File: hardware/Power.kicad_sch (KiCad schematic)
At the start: 1 part

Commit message: added more stuff wip
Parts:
- added C33, C38: 1u, Capacitor_SMD:C_0603_1608Metric, symbol Device:C
- added C34, C38: 0.1u, Capacitor_SMD:C_0603_1608Metric, symbol Device:C
- added C35: 220n, Capacitor_SMD:C_0603_1608Metric, symbol Device:C
- added C37 (x2): 10u, Capacitor_SMD:C_0805_2012Metric, symbol Device:C
- added D16: SMAF4758A, UTSVT_Passives:SODFL4724X108N, symbol Device:D_Zener
- added IC3: LM74502HDDFR, UTSVT_Power:SOT65P280X110-8N, symbol UTSVT_ICs:LM74502HDDFR
- added LVPWR1: LED, LED_SMD:LED_0603_1608Metric, symbol Device:LED
- added Q12, Q13: NVMFWS1D7N04XMT1G, UTSVT_Power:NVMFWS3D0P04M8LT1G, symbol UTSVT_Power:NVMFWS1D7N04XMT1G
- added R36: 10k, Resistor_SMD:R_0603_1608Metric, symbol Device:R_US
- added R37: 200k, Resistor_SMD:R_0603_1608Metric, symbol Device:R_US
- added R38: 9k, Resistor_SMD:R_0603_1608Metric, symbol Device:R_US
- added R83: 4.3k, Resistor_SMD:R_0603_1608Metric, symbol Device:R_US
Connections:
- net +24V_In renamed LV_OUT
- net LV_OUT: now also C37.1, C37.1, C38.1, Q12.5 (D), Q12.6 (D), Q12.7 (D), Q12.8 (D), Q12.9 (D), R83.1
- net +24V_In_Fused renamed 24V_BPS
- new net: C35.2, IC3.4 (VCAP)
- new net: IC3.6 (GATE), Q12.4 (G), Q13.4 (G)
- new net: IC3.7 (OV), R37.2, R38.1
- new net: IC3.8 (SRC), Q12.1 (S), Q12.2 (S), Q12.3 (S), Q13.1 (S), Q13.2 (S), Q13.3 (S)
- new net: LVPWR1.2 (A), R83.2
- new net GND: C33.1, C34.2, C37.2, C37.2, C38.2, C38.2, D16.2 (A), IC3.2 (GND), LVPWR1.1 (K), R38.2
- new net LV+_IN: C34.1, C38.1, Q13.5 (D), Q13.6 (D), Q13.7 (D), Q13.8 (D), Q13.9 (D), R36.1, R37.1
- new net RPP_EN: C33.2, C35.1, D16.1 (K), IC3.1 (EN/UVLO), IC3.5 (VS), R36.2
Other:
- added sheet Power_3V3Buck (Power_3V3Buck.kicad_sch)
- added sheet Power_Protection (Power_Protection.kicad_sch)
- note added: "24V Input Bypass Cap"
- note added: "Fused 24V to other BPS boards"
- note added: "LV PWR indicator LED"
- note added: "Overvoltage Protection: 29.03V Vovr = (R2 * Vov)/(R1 + R2) Vov = Vovr * (R1 + R2) / R2 29.03 = 1.25 * (200k + 9k) / 9k"
- note added: "RPP Protection"
- moved on the sheet: F1

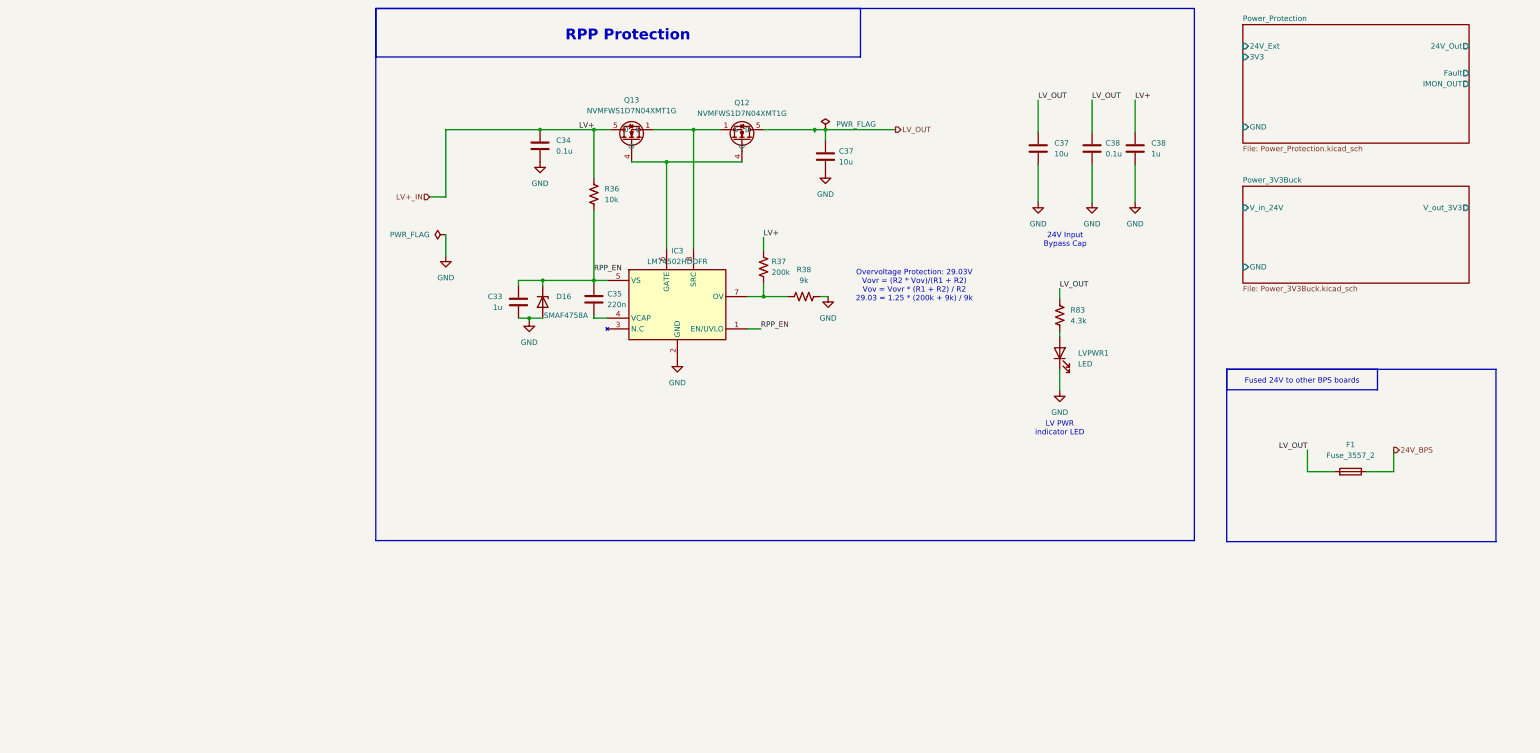
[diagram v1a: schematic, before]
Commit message: some changes - switched to contactor design block - switched to power protection design block - added SD card - added fan I2C pullup - added resistors for ESP32 power mux - shield tied to gnd with 0 ohm - added USB-PD and boost design blocks
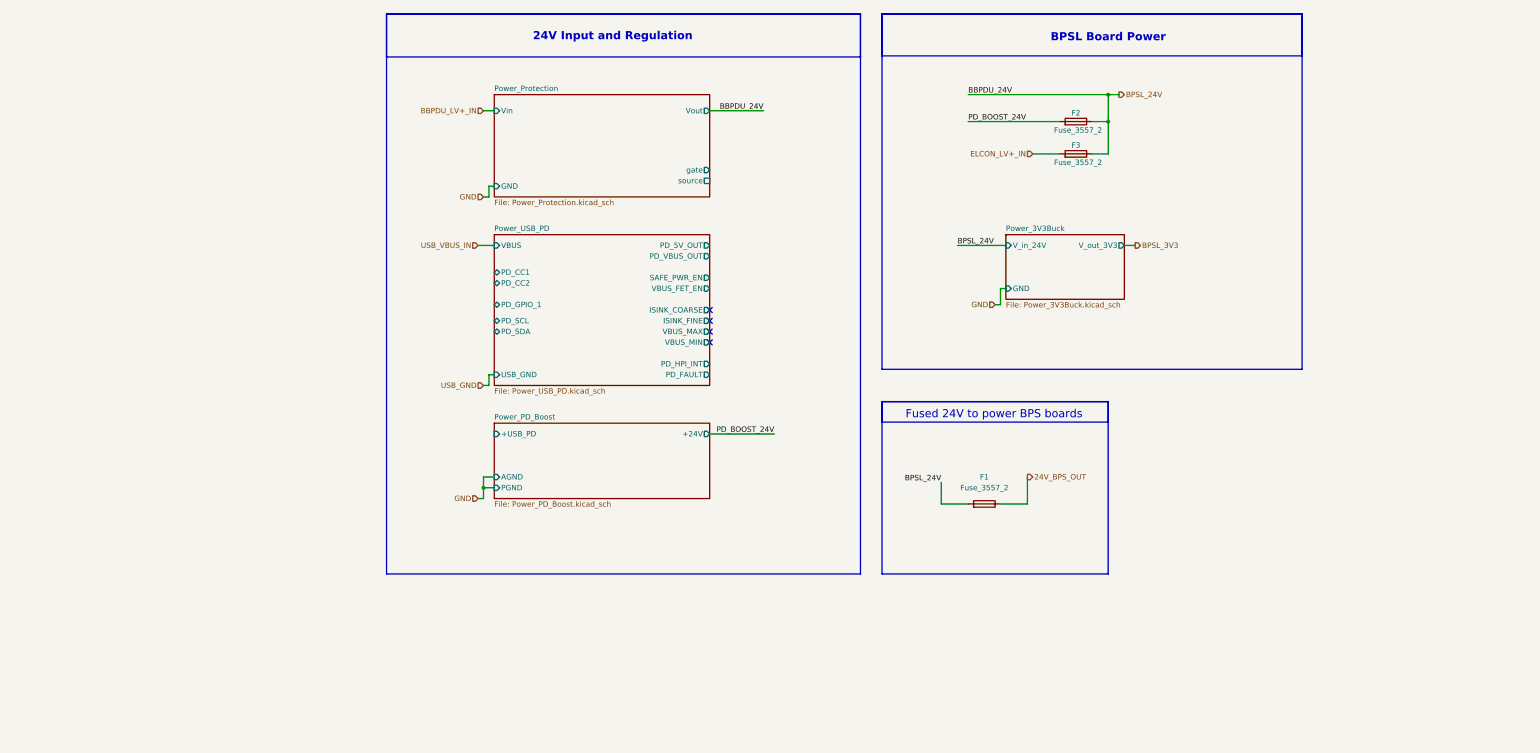
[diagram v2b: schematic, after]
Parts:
- removed C33, C38: 1u, Capacitor_SMD:C_0603_1608Metric, symbol Device:C
- removed C34, C38: 0.1u, Capacitor_SMD:C_0603_1608Metric, symbol Device:C
- removed C35: 220n, Capacitor_SMD:C_0603_1608Metric, symbol Device:C
- removed C37 (x2): 10u, Capacitor_SMD:C_0805_2012Metric, symbol Device:C
- removed D16: SMAF4758A, UTSVT_Passives:SODFL4724X108N, symbol Device:D_Zener
- removed IC3: LM74502HDDFR, UTSVT_Power:SOT65P280X110-8N, symbol UTSVT_ICs:LM74502HDDFR
- removed LVPWR1: LED, LED_SMD:LED_0603_1608Metric, symbol Device:LED
- removed Q12, Q13: NVMFWS1D7N04XMT1G, UTSVT_Power:NVMFWS3D0P04M8LT1G, symbol UTSVT_Power:NVMFWS1D7N04XMT1G
- removed R36: 10k, Resistor_SMD:R_0603_1608Metric, symbol Device:R_US
- removed R37: 200k, Resistor_SMD:R_0603_1608Metric, symbol Device:R_US
- removed R38: 9k, Resistor_SMD:R_0603_1608Metric, symbol Device:R_US
- removed R83: 4.3k, Resistor_SMD:R_0603_1608Metric, symbol Device:R_US
- added F2, F3: Fuse_3557_2, LHRS_Power:Fuse-3557-2, symbol lhrs_power:Fuse_3557_2
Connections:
- net 24V_BPS renamed 24V_BPS_OUT
- net LV_OUT renamed BPSL_24V
- net BPSL_24V: now also F2.2, F3.2
- new net ELCON_LV+_IN: F3.1
- new net PD_BOOST_24V: F2.1
- no-connect marks 0 -> 4
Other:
- added sheet Power_PD_Boost (Power_PD_Boost.kicad_sch)
- added sheet Power_USB_PD (Power_USB_PD.kicad_sch)
- sheet Power_Protection ports: added Vin, Vout, gate, source; removed 24V_Ext, 24V_Out, 3V3, Fault, IMON_OUT
- note added: "24V Input and Regulation"
- note added: "BPSL Board Power"
- note added: "Fused 24V to power BPS boards"
- note removed: "24V Input Bypass Cap"
- note removed: "Fused 24V to other BPS boards"
- note removed: "LV PWR indicator LED"
- note removed: "Overvoltage Protection: 29.03V Vovr = (R2 * Vov)/(R1 + R2) Vov = Vovr * (R1 + R2) / R2 29.03 = 1.25 * (200k + 9k) / 9k"
- note removed: "RPP Protection"
- moved on the sheet: F1

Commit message: power updates
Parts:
- added R28: 16k, symbol Device:R_Small
- added R29: 4.7k, symbol Device:R_Small
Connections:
- net BPSL_24V: no longer F2.2, F3.2
- net GND: now also R29.2
- new net PD_5V_OUT: R28.1
- new net Power_5VMux/PR1: R28.2, R29.1
- no-connect marks 4 -> 0
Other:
- removed sheet Power_3V3Buck
- added sheet Power_3V3_LDO (Power_3V3_LDO.kicad_sch)
- added sheet Power_5VBuck (Power_5VBuck.kicad_sch)
- added sheet Power_5VMux (Power_5VMux.kicad_sch)
- note added: "5V Mux"
- note added: "BPSL Board Power (24V, 3V3)"
- note added: "Mux?"
- note added: "PDU Regulation (RPP)"
- note added: "R1"
- note added: "R2"
- note added: "USB PD + Boost"
- note added: "VIN1 prioritized"
- note removed: "BPSL Board Power"
- moved on the sheet: F1, F2, F3

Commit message: interview tabling
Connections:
- net 24V_BPS_OUT renamed 12V_BPS_OUT
- net BPSL_24V renamed BPSL_12V
- net PD_BOOST_24V renamed PD_12V
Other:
- note added: "((PDU | ELCON) | PD) reasoning: PDU or elcon will be prioritized over PD since it could be being used for debugging. In those events, power from car or elcon is better. since PD needs the lowest priority, it will be one its own input into the highest mux so the other input will have higher priority. then, between PDU and ELCON that mux can prioritize PDU"
- note added: "12V Input and Regulation"
- note added: "BPSL Board Power (12V, 3V3)"
- note added: "Fused 12V to power BPS boards"
- note added: "PD should try to negotiate 12V. Or could just try to negotiate highest possible and rely on buckboost"
- note removed: "24V Input and Regulation"
- note removed: "BPSL Board Power (24V, 3V3)"
- note removed: "Fused 24V to power BPS boards"
- moved on the sheet: R28, R29

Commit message: asdf
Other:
- added sheet 12VPowerMux (Power_Mux_12V.kicad_sch)
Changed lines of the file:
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@@
+	)
+	(sheet
+		(at 111.125 102.87)
+		(size 20.32 20.955)
+		(exclude_from_sim no)
+		(in_bom yes)
+		(on_board yes)
+		(dnp no)
+		(fields_autoplaced yes)
+		(stroke
+			(width 0.1524)
+			(type solid)
+		)
+		(fill
+			(color 0 0 0 0)
+		)
+		(property "Sheetname" "12VPowerMux"
+			(at 111.125 102.1584 0)
+			(show_name no)
+			(do_not_autoplace no)
+			(effects
+				(font
+					(size 1.27 1.27)
+				)
+				(justify left bottom)
+			)
+		)
+		(property "Sheetfile" "Power_Mux_12V.kicad_sch"
+			(at 111.125 124.4096 0)
+			(show_name no)
+			(do_not_autoplace no)
+			(effects
+				(font
+					(size 1.27 1.27)
+				)
+				(justify left top)
+			)
+		)
+		(instances
+			(project "PS-BPSLeader"
+				(path "/d4a4ed4f-0983-4aef-b212-0e3284ab3963/69244dac-f10b-499c-a2b2-3cdf1370aa1f"
+					(page "10")
+				)
+			)
+		)
 	)
 	(sheet

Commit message: end of workday
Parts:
- removed F1: Fuse_3557_2, UTSVT_Power:Fuse-3557-2, symbol utsvt_power:Fuse_3557_2
- added TP?: PD_5V, symbol Connector:TestPoint
- added TP?: MUX_12V, symbol Connector:TestPoint
- added TP?: PDU_ELCON, symbol Connector:TestPoint
- added TP?: PD_OUT, symbol Connector:TestPoint
- F2, F3: value Fuse_3557_2 -> 5A
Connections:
- net PD_5V_OUT: now also TP?.1
- net Power_Mux_PDU_ELCON/Vin2: now reaches F3.2
- net Power_Mux_PD/Vin2: now reaches F2.2
- net PD_12V renamed USB_PD_OUT
- net USB_PD_OUT: now also TP?.1
- new net Power_Mux_PD/12V_MUX_OUT: TP?.1
- new net Power_Mux_PD/Vin1: TP?.1
- no-connect marks 0 -> 10
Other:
- sheet 12VPowerMux renamed Power_Mux_PDU_ELCON
- removed sheet Power_5VBuck
- removed sheet Power_PD_Boost
- removed sheet Power_Protection
- added sheet 12VBuck (12VBuck.kicad_sch)
- added sheet Power_Mux_PD (Power_Mux_PD.kicad_sch)
- sheet Power_Mux_PDU_ELCON ports: added 12V_MUX_OUT, GND, Vin1, Vin2; removed none
- note added: "((PDU | ELCON) | PD) reasoning: PDU or elcon will be prioritized over PD since it could be being used for debugging. In those events, power from car or elcon is better. since PD is the lowest priority, it will be one its own input into the highest mux so the other input will have higher priority. then, between PDU and ELCON that mux can prioritize PDU"
- note added: "USB PD"
- note removed: "((PDU | ELCON) | PD) reasoning: PDU or elcon will be prioritized over PD since it could be being used for debugging. In those events, power from car or elcon is better. since PD needs the lowest priority, it will be one its own input into the highest mux so the other input will have higher priority. then, between PDU and ELCON that mux can prioritize PDU"
- note removed: "Fused 12V to power BPS boards"
- note removed: "Mux?"
- note removed: "USB PD + Boost"
- moved on the sheet: F2, F3, R28, R29

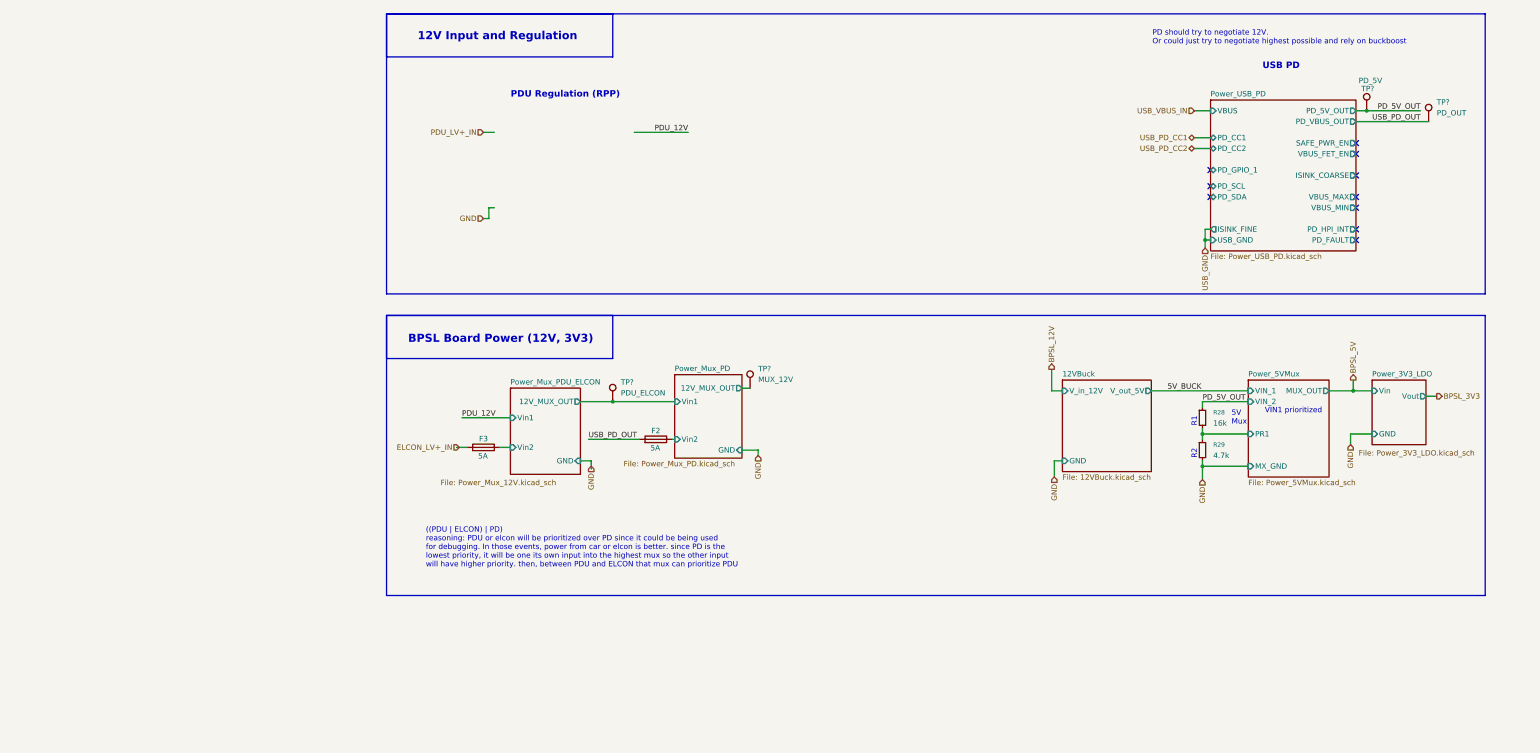
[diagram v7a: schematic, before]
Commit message: finished schematic except for 12v buck boost
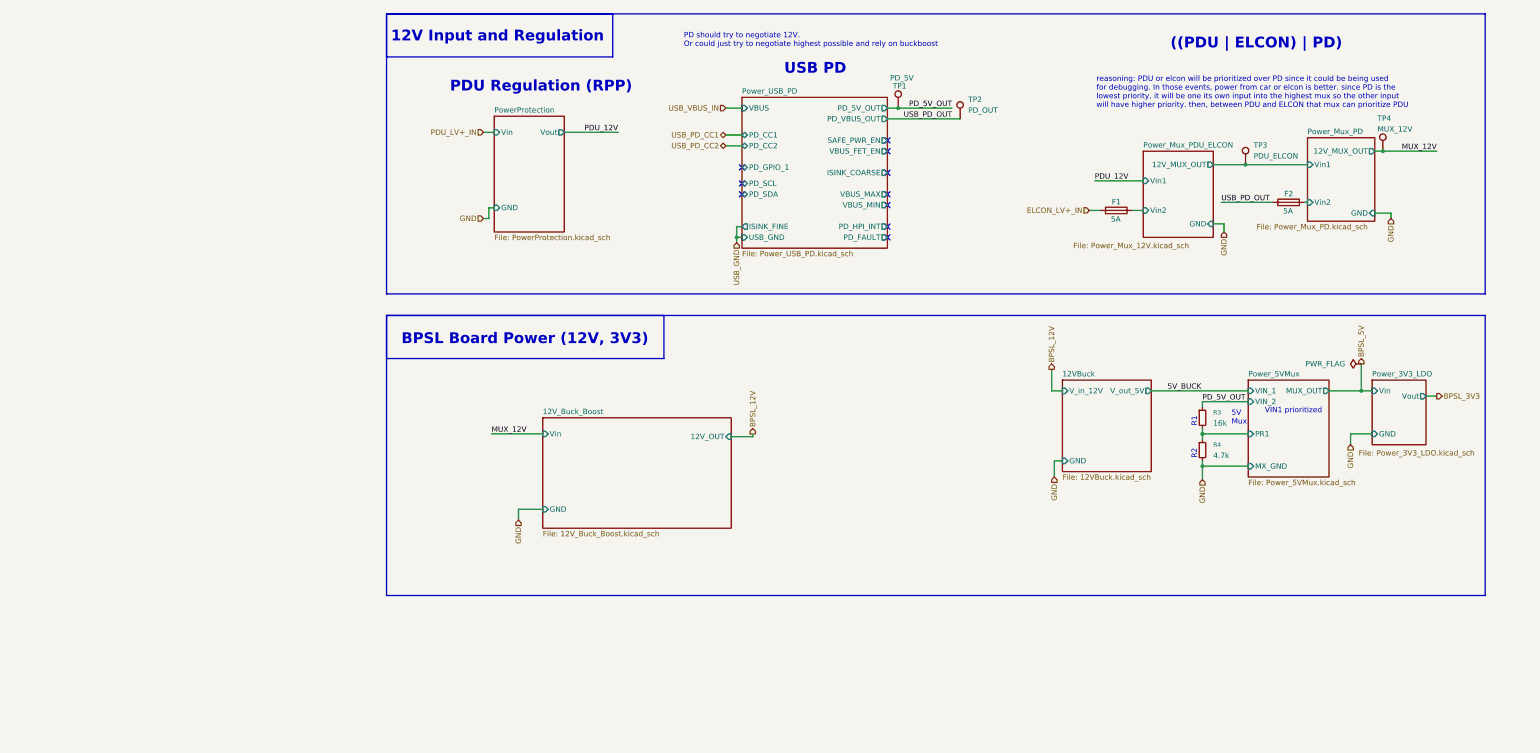
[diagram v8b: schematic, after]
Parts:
- R3: renamed from R28; footprint (none) -> Resistor_SMD:R_0603_1608Metric_Pad0.98x0.95mm_HandSolder
- R4: renamed from R29; footprint (none) -> Resistor_SMD:R_0603_1608Metric_Pad0.98x0.95mm_HandSolder
- TP1, TP3, TP4: renamed from TP?; footprint (none) -> TestPoint:TestPoint_Loop_D2.50mm_Drill1.0mm
- TP2: renamed from TP?; footprint (none) -> TestPoint:TestPoint_Loop_D1.80mm_Drill1.0mm_Beaded
- renumbered F3 to F1
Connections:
- net Power_Mux_PD/12V_MUX_OUT renamed MUX_12V
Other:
- added sheet 12V_Buck_Boost (12V_Buck_Boost.kicad_sch)
- added sheet PowerProtection (PowerProtection.kicad_sch)
- note added: "((PDU | ELCON) | PD)"
- note added: "reasoning: PDU or elcon will be prioritized over PD since it could be being used for debugging. In those events, power from car or elcon is better. since PD is the lowest priority, it will be one its own input into the highest mux so the other input will have higher priority. then, between PDU and ELCON that mux can prioritize PDU"
- note removed: "((PDU | ELCON) | PD) reasoning: PDU or elcon will be prioritized over PD since it could be being used for debugging. In those events, power from car or elcon is better. since PD is the lowest priority, it will be one its own input into the highest mux so the other input will have higher priority. then, between PDU and ELCON that mux can prioritize PDU"
- moved on the sheet: F1, F2, TP1, TP2, TP3, TP4
